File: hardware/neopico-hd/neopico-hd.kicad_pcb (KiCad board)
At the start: 2 copper layers, 11 parts, among them J1 HDMI_A, U1 SN74LVC2G14DBV, U2 SN74LVC2G14DBV, U3 SN74LVC245APW, U4 SN74LVC245APW, U5 SN74LVC245APW, U6 ESD224DQA, U7 ESD224DQA

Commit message: Starting PCB
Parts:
- removed U6, U7: ESD224DQA, Package_DFN_QFN:Diodes_UDFN-10_1.0x2.5mm_P0.5mm
- added J2: Conn_01x05_Socket, Connector_JST:JST_XH_B5B-XH-A_1x05_P2.50mm_Vertical, F.Cu at (115.5, 30.0)
- added J3: Conn_01x05_Socket, Connector_JST:JST_XH_B5B-XH-A_1x05_P2.50mm_Vertical, F.Cu at (105.6, 47.7)
- added J4: Conn_01x05_Socket, Connector_JST:JST_XH_B5B-XH-A_1x05_P2.50mm_Vertical, F.Cu at (94.1, 77.5)
- moved A1 89.1 mm to (211.0, 70.0), turned to -90 degrees
- moved U3 82.2 mm to (143.2, 43.1)
- moved C6 66.9 mm to (220.0, 132.5)
- moved J1 44.5 mm to (206.0, 29.2), turned to 90 degrees
- moved D1 37.3 mm to (116.9, 99.2)
- moved U1 37.3 mm to (115.4, 110.5)
- moved U2 37.3 mm to (115.4, 115.1)
- moved U4 37.3 mm to (108.5, 109.0)
- moved U5 37.3 mm to (108.5, 117.1)
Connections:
- A1 pad 18: D2+ -> CLK-
- A1 pad 19: D2- -> CLK+
- A1 pad 20: D1+ -> D0-
- A1 pad 21: D1- -> D0+
- A1 pad 22: D0+ -> D1-
- A1 pad 23: D0- -> D1+
- A1 pad 24: CLK+ -> D2-
- A1 pad 25: CLK- -> D2+
- A1 pad 37: SHADOW -> SHD
- J1 pad 1: HDMI_D2+ -> D2+
- J1 pad 10: HDMI_CLK+ -> CLK+
- J1 pad 12: HDMI_CLK- -> CLK-
- J1 pad 3: HDMI_D2- -> D2-
- J1 pad 4: HDMI_D1+ -> D1+
- J1 pad 6: HDMI_D1- -> D1-
- J1 pad 7: HDMI_D0+ -> D0+
- J1 pad 9: HDMI_D0- -> D0-
- U5 pad 15: unconnected-(U5-B4-Pad15) -> WS
- U5 pad 16: unconnected-(U5-B3-Pad16) -> DAT
- U5 pad 17: WS -> SHD
- U5 pad 18: DAT -> DARK
- U5 pad 2: MVS_DAT -> MVS_DARK
- U5 pad 3: MVS_WS -> MVS_SHD
- U5 pad 4: unconnected-(U5-A3-Pad4) -> MVS_DAT
- U5 pad 5: unconnected-(U5-A4-Pad5) -> MVS_WS
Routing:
- net CLK-: track 0.00 -> 24.5 mm
- net D2-: track 0.00 -> 24.0 mm
- net D1-: track 0.00 -> 23.6 mm
- net D0-: track 0.00 -> 23.5 mm
- net CLK+: track 0.00 -> 22.2 mm
- net D2+: track 0.00 -> 21.9 mm
- net D1+: track 0.00 -> 21.5 mm
- net D0+: track 0.00 -> 21.2 mm

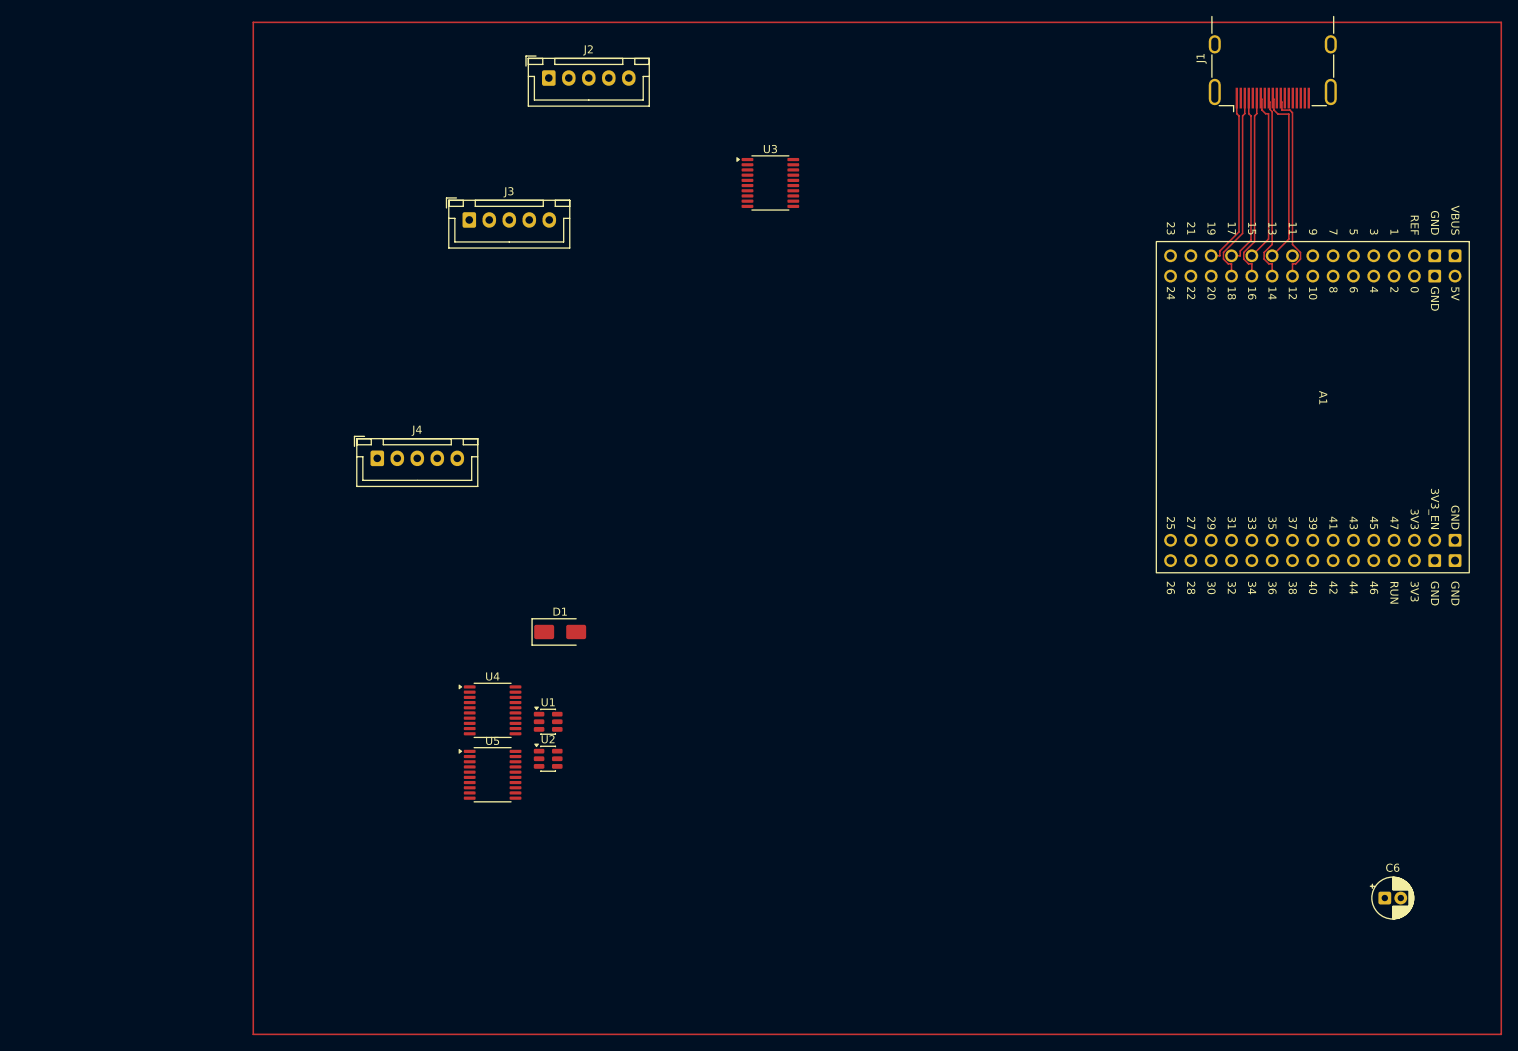
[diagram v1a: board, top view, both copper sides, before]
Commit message: GP25+ video capture working
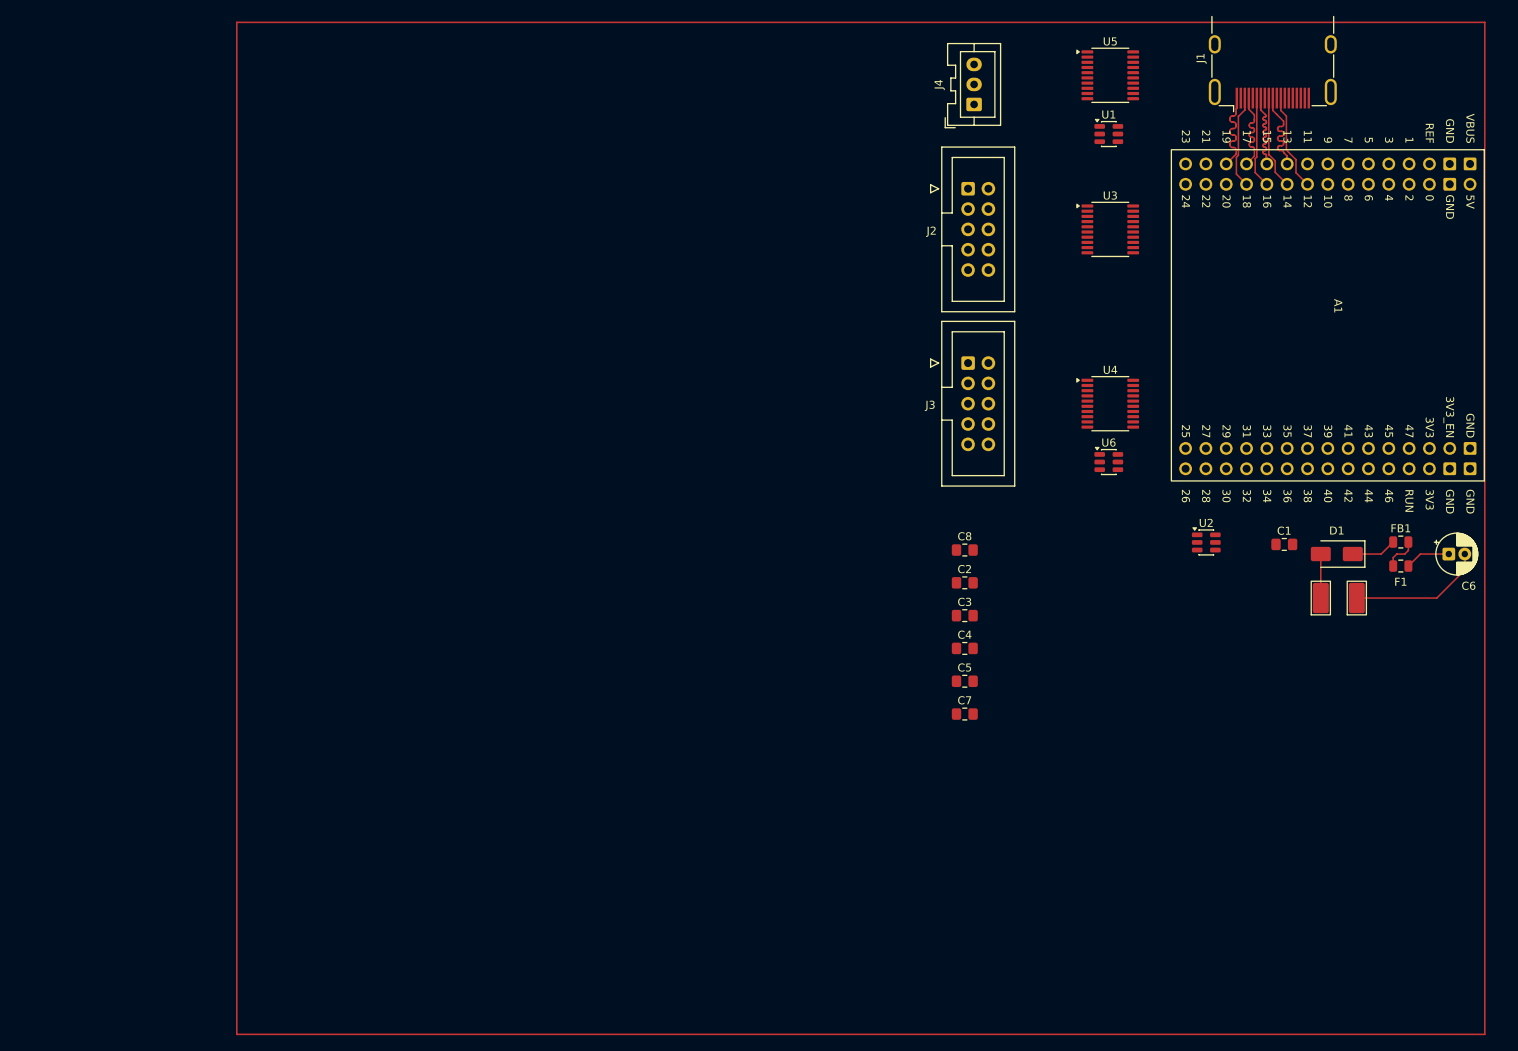
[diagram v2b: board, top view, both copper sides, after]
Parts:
- added C1: 0.1u, Capacitor_SMD:C_0805_2012Metric_Pad1.18x1.45mm_HandSolder, F.Cu at (207.4, 88.3)
- added C2: 0.1u, Capacitor_SMD:C_0805_2012Metric_Pad1.18x1.45mm_HandSolder, F.Cu at (167.5, 93.1)
- added C3: 0.1u, Capacitor_SMD:C_0805_2012Metric_Pad1.18x1.45mm_HandSolder, F.Cu at (167.5, 97.2)
- added C4: 0.1u, Capacitor_SMD:C_0805_2012Metric_Pad1.18x1.45mm_HandSolder, F.Cu at (167.5, 101.3)
- added C5: 0.1u, Capacitor_SMD:C_0805_2012Metric_Pad1.18x1.45mm_HandSolder, F.Cu at (167.5, 105.4)
- added C7: 0.1u, Capacitor_SMD:C_0805_2012Metric_Pad1.18x1.45mm_HandSolder, F.Cu at (167.5, 109.5)
- added C8: 0.1u, Capacitor_SMD:C_0805_2012Metric_Pad1.18x1.45mm_HandSolder, F.Cu at (167.5, 89.0)
- added F1: Polyfuse, Capacitor_SMD:C_0805_2012Metric, F.Cu at (222.0, 91.0)
- added FB1: FerriteBead, Capacitor_SMD:C_0805_2012Metric, F.Cu at (222.0, 88.0)
- added REF**: TestPoint_Keystone_5019_Miniature, TestPoint:TestPoint_Keystone_5019_Miniature, F.Cu at (216.5, 95.0)
- added REF**: TestPoint_Keystone_5019_Miniature, TestPoint:TestPoint_Keystone_5019_Miniature, F.Cu at (212.0, 95.0)
- added U6: V_BUFF, Package_TO_SOT_SMD:SOT-23-6, F.Cu at (185.5, 78.0)
- J2, J3: value Conn_01x05_Socket -> Conn_02x05_Top_Bottom; footprint Connector_JST:JST_XH_B5B-XH-A_1x05_P2.50mm_Vertical -> Connector_IDC:IDC-Header_2x05_P2.54mm_Vertical
- J4: value Conn_01x05_Socket -> Audio; footprint Connector_JST:JST_XH_B5B-XH-A_1x05_P2.50mm_Vertical -> Connector_JST:JST_XA_B03B-XASK-1_1x03_P2.50mm_Vertical
- U1: value SN74LVC2G14DBV -> A_BUFF
- U2: value SN74LVC2G14DBV -> V_BUFF
- U3: value SN74LVC245APW -> RG_LVS
- U4: value SN74LVC245APW -> GB_LVS
- U5: value SN74LVC245APW -> AV_LVS
- moved U5 116.6 mm to (185.7, 29.7)
- moved U1 101.5 mm to (185.5, 37.0)
- moved D1 97.6 mm to (214.0, 89.5), turned to 180 degrees
- moved J4 86.7 mm to (168.7, 33.3), turned to 90 degrees
- moved U2 86.6 mm to (197.7, 88.0)
- moved U4 86.2 mm to (185.7, 70.7)
- moved J3 64.9 mm to (167.9, 65.6)
- moved J2 54.2 mm to (167.9, 43.8)
- moved C6 43.7 mm to (228.0, 89.5)
- moved U3 42.9 mm to (185.7, 48.9)
- moved A1 11.6 mm to (212.9, 58.5)
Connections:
- A1 pad 28: unconnected-(A1-GPIO23-Pad28) -> DAT
- A1 pad 29: unconnected-(A1-GPIO23-Pad29) -> WS
- A1 pad 30: unconnected-(A1-GPIO24-Pad30) -> BCK
- A1 pad 6: DAT -> unconnected-(A1-GPIO0-Pad6)
- A1 pad 7: WS -> unconnected-(A1-GPIO1-Pad7)
- A1 pad 8: BCK -> unconnected-(A1-GPIO2-Pad8)
- J1 pad 18: +5V -> +5V FILTERED
- J3 pad 1: MVS_G0 -> MVS_B0
- J3 pad 2: MVS_G1 -> MVS_B1
- J3 pad 3: MVS_G2 -> MVS_B2
- J3 pad 4: MVS_G3 -> MVS_B3
- J3 pad 5: MVS_G4 -> MVS_B4
- J4 pad 1: MVS_B0 -> MVS_BCK
- J4 pad 2: MVS_B1 -> MVS_WS
- J4 pad 3: MVS_B2 -> MVS_DAT
- U4 pad 11: F0 -> unconnected-(U4-B8-Pad11)
- U4 pad 9: MVS_F0 -> unconnected-(U4-A8-Pad9)
- U5 pad 15: WS -> unconnected-(U5-B4-Pad15)
- U5 pad 16: DAT -> unconnected-(U5-B3-Pad16)
- U5 pad 17: SHD -> WS
- U5 pad 18: DARK -> DAT
- U5 pad 2: MVS_DARK -> MVS_DAT
- U5 pad 3: MVS_SHD -> MVS_WS
- U5 pad 4: MVS_DAT -> unconnected-(U5-A3-Pad4)
- U5 pad 5: MVS_WS -> unconnected-(U5-A4-Pad5)
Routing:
- net GND: track 0.00 -> 16.9 mm
- net CLK-: track 24.5 -> 12.2 mm
- net D2-: track 24.0 -> 11.7 mm
- net D1-: track 23.6 -> 11.5 mm
- net D0-: track 23.5 -> 11.7 mm
- net D2+: track 21.9 -> 11.6 mm
- net CLK+: track 22.2 -> 12.1 mm
- net D1+: track 21.5 -> 11.4 mm
- net D0+: track 21.2 -> 11.6 mm
- net Net-(D1-K): track 0.00 -> 5.67 mm
- net +5V FILTERED: track 0.00 -> 5.67 mm
- net +5V MVS: track 0.00 -> 5.50 mm
- net Net-(F1-Pad1): track 0.00 -> 4.37 mm
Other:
- board text added: "11"
- board text added: "12"
- board text added: "13"
- board text added: "14"
- board text added: "15"
- board text added: "16"
- board text added: "17"
- board text added: "18"
- board text added: "19"
- board text added: "20"
- board text added: "21"
- board text added: "22"
- board text added: "23"
- board text added: "24"
- board text added: "9"
- board text added: "C6"
